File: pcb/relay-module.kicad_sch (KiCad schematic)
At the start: 4 parts

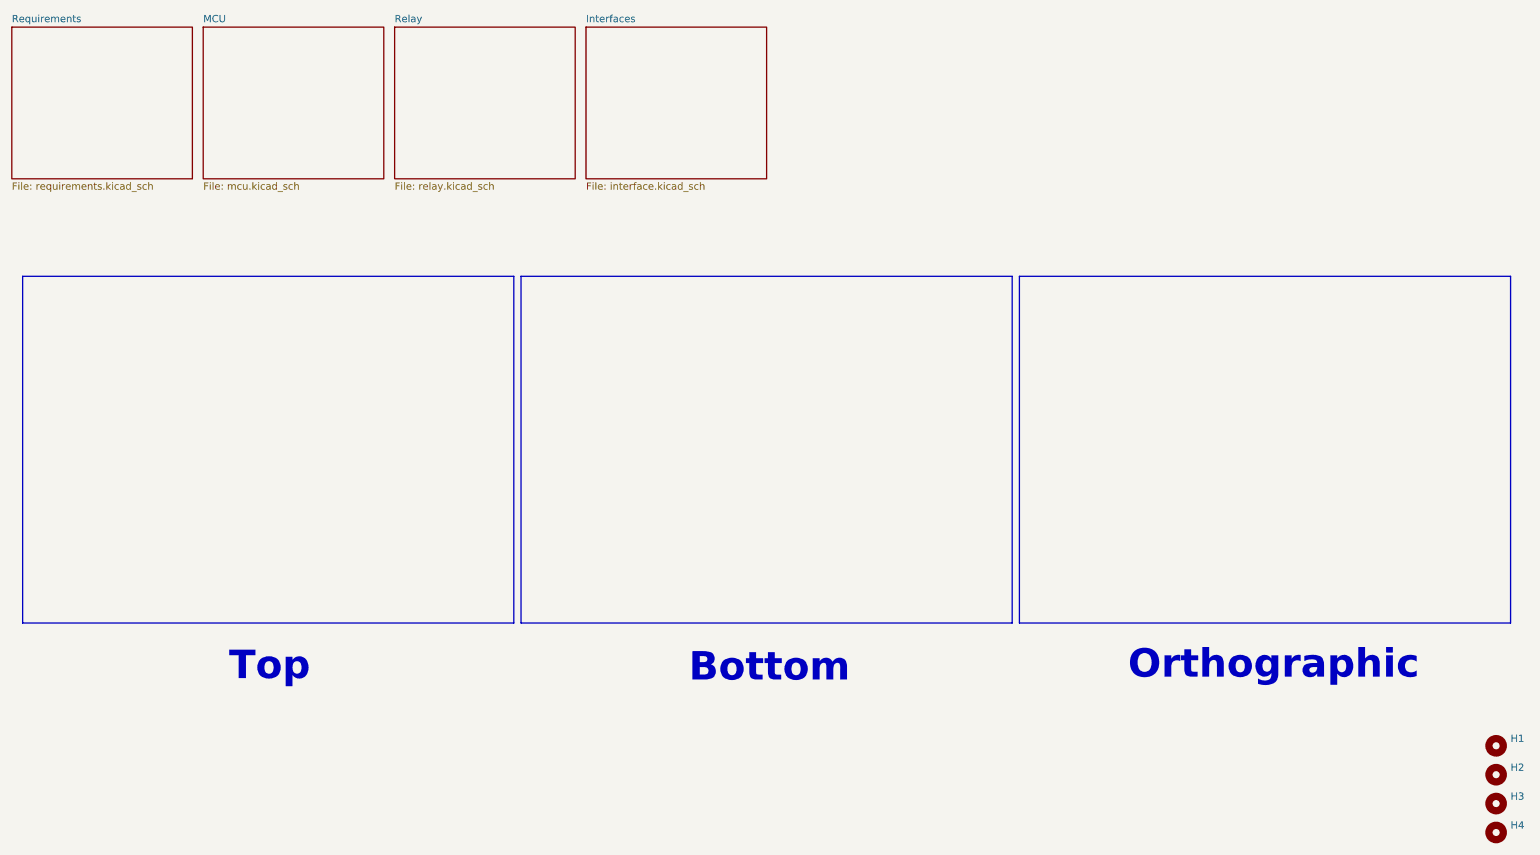
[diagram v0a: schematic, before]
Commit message: Updated for consistency
Updated footprints
Added ESD to power
Added second QWICC connector
Rerouted as required
Made mounting holes grounded
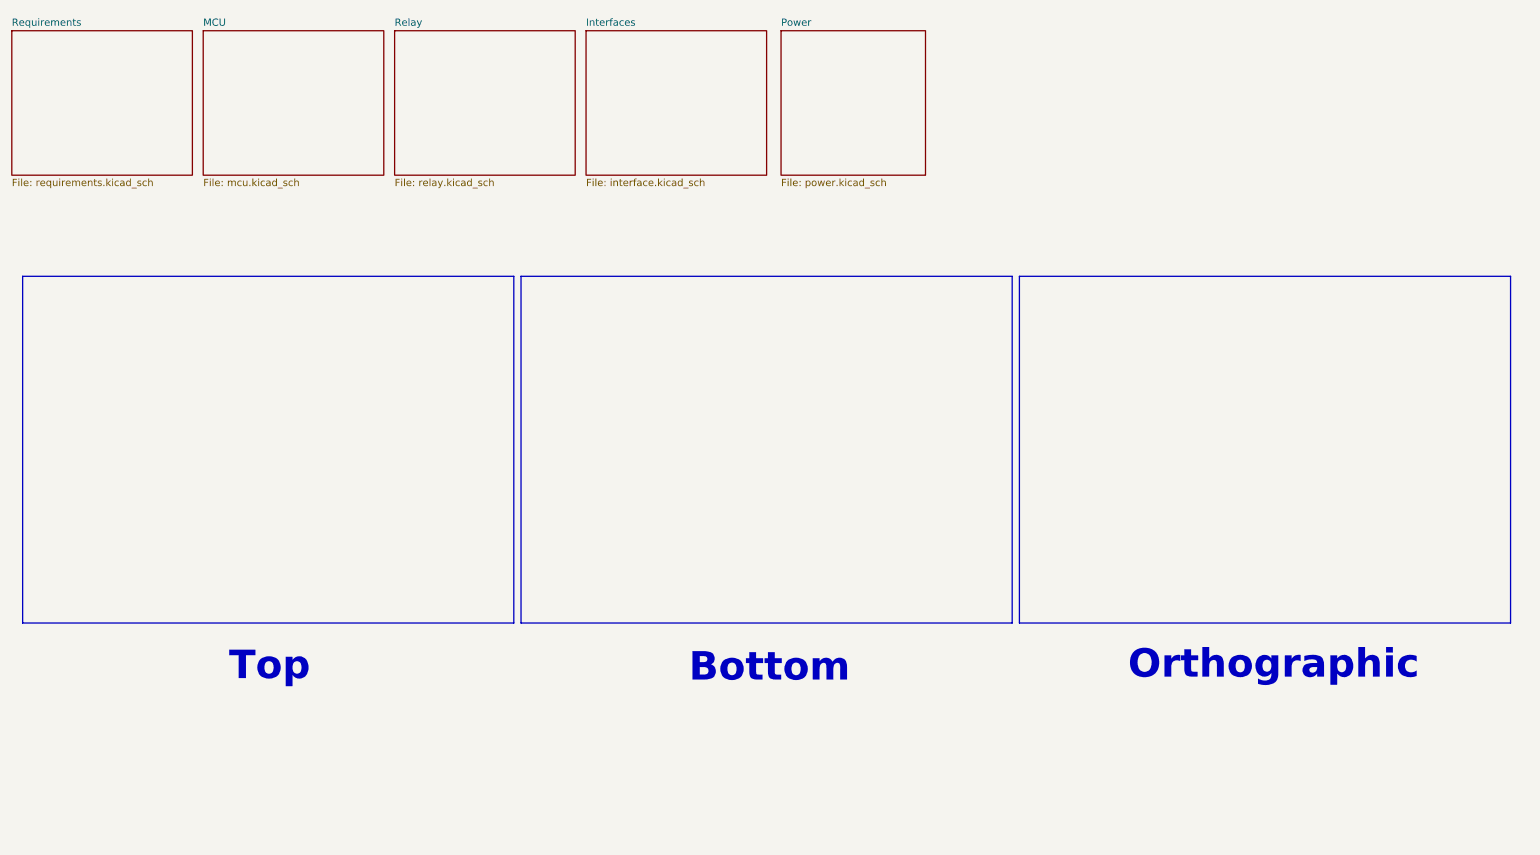
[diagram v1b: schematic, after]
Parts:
- removed H1, H2, H3, H4: MountingHole, CRGM Mechanical:MountingHole_3.2mm_M3_Pad_Via, symbol Mechanical:MountingHole
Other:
- added sheet Power (power.kicad_sch)
